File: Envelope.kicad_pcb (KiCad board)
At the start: 2 copper layers, 39.6 x 100 mm, 54 parts, among them J6 Conn_02x03_Odd_Even, J7 Conn_01x06, J8 Conn_02x05_Odd_Even, SW1 RST, U1 TL072, U2 ATmega328PB-AU, U3 L7805, Y1 Crystal

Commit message: Finished schema and footprint assignments.
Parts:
- removed J6: Conn_02x03_Odd_Even, Pin_Headers:Pin_Header_Straight_2x03_Pitch2.54mm
- removed J7: Conn_01x06, Pin_Headers:Pin_Header_Straight_1x06_Pitch2.54mm
- removed J8: Conn_02x05_Odd_Even, Pin_Headers:Pin_Header_Straight_2x05_Pitch2.54mm
- added C14: 100n, Capacitor_SMD:C_0805_2012Metric, F.Cu at (167.3, 45.5)
- added C15: 10u, Capacitor_SMD:CP_Elec_4x5.8, F.Cu at (162.2, 44.7)
- added C16: 100n, Capacitor_SMD:C_0805_2012Metric, F.Cu at (189.5, 50.0)
- added C17: 100n, Capacitor_SMD:C_0805_2012Metric, F.Cu at (199.1, 44.0)
- added C18: 100n, Capacitor_SMD:C_0805_2012Metric, F.Cu at (192.9, 48.1)
- added C19: 22p, Capacitor_SMD:C_0805_2012Metric, F.Cu at (192.9, 50.0)
- added C20: 22p, Capacitor_SMD:C_0805_2012Metric, F.Cu at (199.1, 40.5)
- added D10: LED, LED_THT:LED_D3.0mm, F.Cu at (192.4, 63.6)
- added D11: LED, LED_THT:LED_D3.0mm, F.Cu at (192.4, 59.1)
- added D12: LED, LED_THT:LED_D3.0mm, F.Cu at (197.3, 59.1)
- added D13: LED, LED_SMD:LED_1206_3216Metric_Castellated, F.Cu at (193.8, 55.7)
- added D9: LED, LED_SMD:LED_1206_3216Metric_Castellated, F.Cu at (168.1, 43.3)
- added J1: Conn_02x05_Odd_Even, Connector_PinHeader_2.54mm:PinHeader_2x05_P2.54mm_Vertical, F.Cu at (147.7, 39.2)
- added J2: Conn_02x03_Odd_Even, Connector_PinHeader_2.54mm:PinHeader_2x03_P2.54mm_Vertical, F.Cu at (203.3, 36.1)
- added J3: Conn_01x06, Connector_PinHeader_2.54mm:PinHeader_1x06_P2.54mm_Vertical, F.Cu at (186.0, 36.1)
- added R16: 100k, Resistor_SMD:R_0805_2012Metric, F.Cu at (128.7, 51.1)
- added R17: 1k, Resistor_SMD:R_0805_2012Metric, F.Cu at (119.0, 63.2)
- added R18: 47k, Resistor_SMD:R_0805_2012Metric, F.Cu at (123.7, 58.6)
- added R19: 47k, Resistor_SMD:R_0805_2012Metric, F.Cu at (135.9, 44.2)
- added R20: 47k, Resistor_SMD:R_0805_2012Metric, F.Cu at (132.3, 48.7)
- added R21: 100k, Resistor_SMD:R_0805_2012Metric, F.Cu at (140.7, 39.6)
- added R22: 1k, Resistor_SMD:R_0805_2012Metric, F.Cu at (120.1, 54.1)
- added R23: 330, Resistor_SMD:R_0805_2012Metric, F.Cu at (164.0, 49.4)
- added R24: 330, Resistor_SMD:R_0805_2012Metric, F.Cu at (202.8, 57.4)
- added R25: 330, Resistor_SMD:R_0805_2012Metric, F.Cu at (198.0, 55.5)
- added R26: 330, Resistor_SMD:R_0805_2012Metric, F.Cu at (201.4, 55.5)
- added R27: 10k, Resistor_SMD:R_0805_2012Metric, F.Cu at (189.5, 48.1)
- added R28: 330, Resistor_SMD:R_0805_2012Metric, F.Cu at (197.9, 62.3)
- added SW2: SW_SPDT_MSM, Local:SP1MS1, F.Cu at (189.5, 60.2)
- added SW3: SW_Push, Button_Switch_THT:SW_PUSH_6mm_H9.5mm, F.Cu at (189.3, 41.1)
- C1, C2, C3: value C -> 47n; footprint Capacitors_SMD:C_0805 -> Capacitor_SMD:C_0805_2012Metric; moved to F.Cu
- C10, C5: footprint Capacitors_SMD:C_0805 -> Capacitor_SMD:C_0805_2012Metric; moved to F.Cu
- C11: value 100n -> 10u; footprint Capacitors_SMD:C_0805 -> Capacitor_SMD:CP_Elec_4x5.8; moved to F.Cu
- C12: footprint Capacitors_SMD:CP_Elec_4x5.8 -> Capacitor_SMD:CP_Elec_4x5.8; moved to F.Cu
- C13, C9: value 10u -> 100n; footprint Capacitors_SMD:CP_Elec_4x5.8 -> Capacitor_SMD:C_0805_2012Metric; moved to F.Cu
- C4: value 100n -> 47n; footprint Capacitors_SMD:C_0805 -> Capacitor_SMD:C_0805_2012Metric; moved to F.Cu
- C6: value 100n -> 470p; footprint Capacitors_SMD:C_0805 -> Capacitor_SMD:C_0805_2012Metric; moved to F.Cu
- C7: value 22p -> 100n; footprint Capacitors_SMD:C_0805 -> Capacitor_SMD:C_0805_2012Metric; moved to F.Cu
- C8: value 22p -> 470p; footprint Capacitors_SMD:C_0805 -> Capacitor_SMD:C_0805_2012Metric; moved to F.Cu
- D1, D2, D3, D4, D5, D6: footprint Diodes_SMD:D_SOD-123 -> Diode_SMD:D_SOD-123; moved to F.Cu
- D7, D8: footprint Diodes_SMD:D_PowerDI-123 -> Diode_SMD:D_PowerDI-123; moved to F.Cu
- R1, R3: value 47k -> 33k; footprint Resistors_SMD:R_0805 -> Resistor_SMD:R_0805_2012Metric; moved to F.Cu
- R10, R9: value 100k -> 1k; footprint Resistors_SMD:R_0805 -> Resistor_SMD:R_0805_2012Metric; moved to F.Cu
- R11: value 1k -> 47k; footprint Resistors_SMD:R_0805 -> Resistor_SMD:R_0805_2012Metric; moved to F.Cu
- R12: value 100k -> 47k; footprint Resistors_SMD:R_0805 -> Resistor_SMD:R_0805_2012Metric; moved to F.Cu
- R13, R8: footprint Resistors_SMD:R_0805 -> Resistor_SMD:R_0805_2012Metric; moved to F.Cu
- R14: value 4k7 -> 47k; footprint Resistors_SMD:R_0805 -> Resistor_SMD:R_0805_2012Metric; moved to F.Cu
- R15: value 10k -> 47k; footprint Resistors_SMD:R_0805 -> Resistor_SMD:R_0805_2012Metric; moved to F.Cu
- R2, R4: value 4k7 -> 33k; footprint Resistors_SMD:R_0805 -> Resistor_SMD:R_0805_2012Metric; moved to F.Cu
- R5, R6: value R -> 33k; footprint Resistors_SMD:R_0805 -> Resistor_SMD:R_0805_2012Metric; moved to F.Cu
- R7: value R -> 1k; footprint Resistors_SMD:R_0805 -> Resistor_SMD:R_0805_2012Metric; moved to F.Cu
- RV1, RV2, RV3, RV4, RV5: value POT -> 100k; footprint Potentiometers:Potentiometer_Alps_RK09K_Horizontal -> Local:AlpsRK09K
- SW1: value RST -> SW_SPDT_MSM; footprint Buttons_Switches_THT:SW_PUSH_6mm_h13mm -> Local:SP1MS1; moved to F.Cu
- U1: footprint Housings_SSOP:OnSemi_Micro8 -> Package_SO:TSSOP-8_3x3mm_P0.65mm; moved to F.Cu
- U2: footprint Housings_QFP:LQFP-32_7x7mm_Pitch0.8mm -> Package_QFP:TQFP-32_7x7mm_P0.8mm; moved to F.Cu
- U3: footprint TO_SOT_Packages_SMD:TO-263-2 -> Package_TO_SOT_THT:TO-220-3_Vertical; moved to F.Cu
- Y1: value Crystal -> 20MHz; footprint Crystals:Crystal_SMD_5032-2pin_5.0x3.2mm -> Crystal:Crystal_SMD_HC49-SD; moved to F.Cu
- moved D5 135.5 mm to (94.0, 67.4), turned to 0 degrees
- moved D4 132.0 mm to (89.2, 67.4), turned to 0 degrees
- moved D1 126.6 mm to (98.7, 67.4), turned to 0 degrees
- moved R8 121.7 mm to (133.5, 39.6), turned to 0 degrees
- moved R9 121.7 mm to (128.7, 46.5), turned to 0 degrees
- moved D2 119.1 mm to (115.9, 55.3), turned to 0 degrees
- moved D6 116.0 mm to (115.9, 53.0), turned to 0 degrees
- moved R12 115.6 mm to (137.1, 39.6), turned to 0 degrees
- moved D3 115.3 mm to (129.3, 38.5), turned to 0 degrees
- moved C4 115.2 mm to (132.2, 52.0), turned to 0 degrees
- moved R6 113.6 mm to (128.7, 42.0), turned to 0 degrees
- moved R4 113.3 mm to (139.6, 44.2), turned to 0 degrees
- moved R5 113.2 mm to (127.3, 55.6), turned to 0 degrees
- moved R7 111.3 mm to (115.4, 58.8), turned to 0 degrees
- moved C7 110.4 mm to (102.8, 67.2), turned to 0 degrees
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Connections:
- C10 pad 1: +12V -> GND
- C10 pad 2: GND -> -12V
- C11 pad 1: +5V -> +12V
- C12 pad 1: +5V -> GND
- C12 pad 2: GND -> -12V
- C13 pad 1: GND -> +12V
- C13 pad 2: -12V -> GND
- C4 pad 1: +5V -> Net-(C4-Pad1)
- C5 pad 1: GND -> Net-(C5-Pad1)
- C5 pad 2: +5V -> GND
- C6 pad 2: GND -> Net-(C6-Pad2)
- C7 pad 1: GND -> Net-(C7-Pad1)
- C7 pad 2: Net-(C7-Pad2) -> GND
- C8 pad 1: GND -> Net-(C8-Pad1)
- J-Gate1 pad TN: Net-(J-Gate1-PadTN) -> +5V
- J-Trig1 pad TN: Net-(J-Trig1-PadTN) -> +5V
- R10 pad 1: Net-(R10-Pad1) -> Net-(C4-Pad1)
- R10 pad 2: GND -> Net-(C3-Pad1)
- R11 pad 1: Net-(J-Inv1-PadT) -> Net-(C7-Pad1)
- R11 pad 2: Net-(R11-Pad2) -> +5V
- R12 pad 1: Net-(R11-Pad2) -> Net-(C5-Pad1)
- R12 pad 2: GND -> +5V
- R13 pad 1: Net-(D5-Pad2) -> Net-(C6-Pad2)
- R13 pad 2: Net-(J-CV1-PadT) -> Net-(C4-Pad1)
- R14 pad 1: /MCU328/PC5 -> GND
- R14 pad 2: Net-(D5-Pad2) -> Net-(C5-Pad1)
- R15 pad 1: +5V -> Net-(C6-Pad1)
- R15 pad 2: Net-(J6-Pad1) -> Net-(C6-Pad2)
- R2 pad 1: /MCU328/PB0 -> Net-(D3-Pad2)
- R2 pad 2: Net-(D1-Pad2) -> Net-(J-Trig1-PadT)
- R3 pad 1: Net-(D3-Pad2) -> Net-(D5-Pad2)
- R3 pad 2: Net-(J-Trig1-PadT) -> Net-(J-CV1-PadT)
- R4 pad 1: /MCU328/PB2 -> /MCU328/PB0
- R4 pad 2: Net-(D3-Pad2) -> Net-(D1-Pad2)
- R5 pad 1: Net-(C1-Pad1) -> /MCU328/PB2
- R5 pad 2: /MCU328/PB1 -> Net-(D3-Pad2)
- R6 pad 1: Net-(C2-Pad1) -> /MCU328/PC5
- R6 pad 2: Net-(C1-Pad1) -> Net-(D5-Pad2)
- R7 pad 1: Net-(C3-Pad1) -> Net-(C1-Pad1)
- R7 pad 2: Net-(C2-Pad1) -> /MCU328/PB1
- R8 pad 1: Net-(J-Out1-PadT) -> Net-(C2-Pad1)
- R8 pad 2: Net-(R10-Pad1) -> Net-(C1-Pad1)
- R9 pad 2: GND -> Net-(C2-Pad1)
- SW1 pad 1: Net-(J6-Pad1) -> /MCU328/PE0
- U1 pad 1: Net-(R10-Pad1) -> Net-(C6-Pad1)
- U1 pad 2: Net-(R10-Pad1) -> Net-(C6-Pad2)
- U1 pad 3: Net-(C3-Pad1) -> Net-(C5-Pad1)
- U1 pad 5: Net-(U1-Pad5) -> Net-(C7-Pad1)
- U1 pad 6: Net-(U1-Pad6) -> Net-(C8-Pad2)
- U1 pad 7: Net-(R11-Pad2) -> Net-(C8-Pad1)
- U2 pad 16: Net-(J6-Pad1) -> Net-(J2-Pad1)
- U2 pad 17: Net-(J6-Pad1) -> Net-(J2-Pad3)
- U2 pad 20: Net-(C6-Pad1) -> Net-(C16-Pad2)
- U2 pad 29: Net-(J6-Pad1) -> Net-(J2-Pad5)
- U2 pad 7: Net-(C7-Pad2) -> Net-(C19-Pad2)
- U2 pad 8: Net-(C8-Pad2) -> Net-(C20-Pad2)
- Y1 pad 1: Net-(C8-Pad2) -> Net-(C19-Pad2)
- Y1 pad 2: Net-(C7-Pad2) -> Net-(C20-Pad2)
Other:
- board outline removed
- net class Default: via_dia 0.6 -> 0.8
- rule pad_to_mask_clearance: 0.2 -> 0

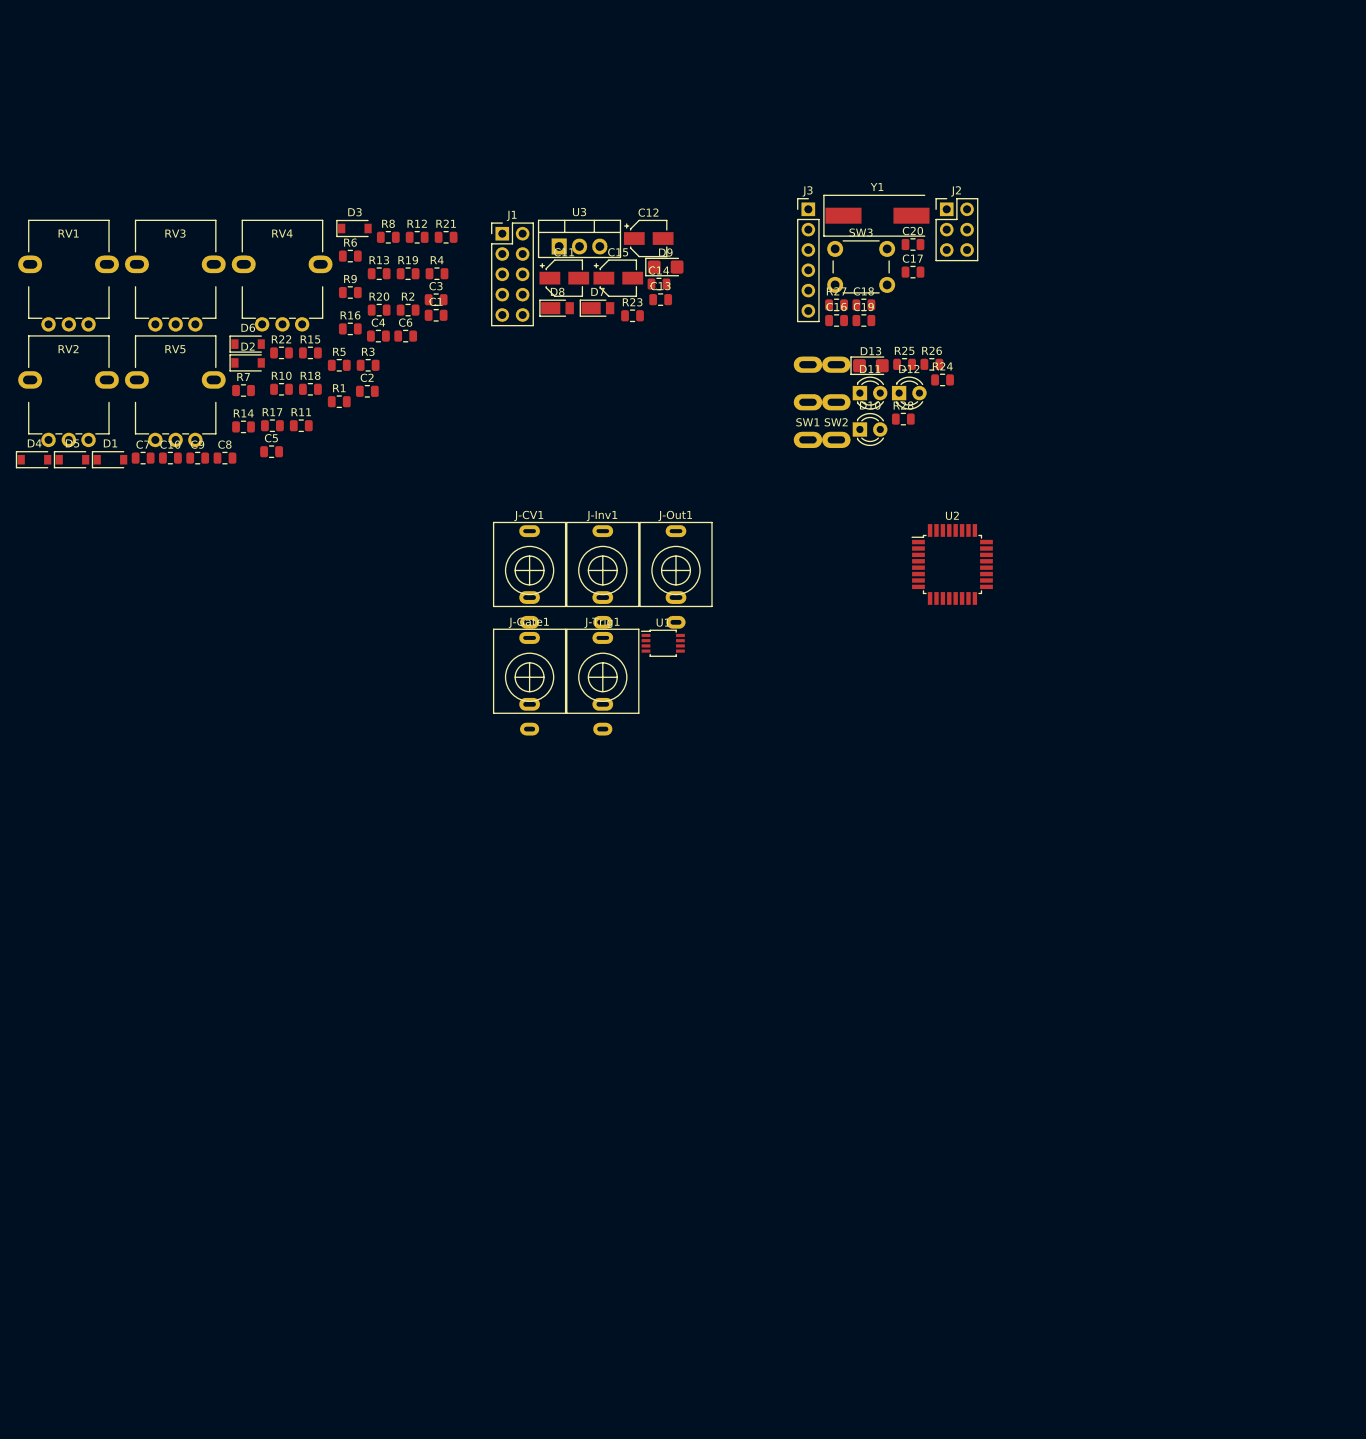
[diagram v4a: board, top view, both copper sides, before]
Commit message: All components place on board but no routing.
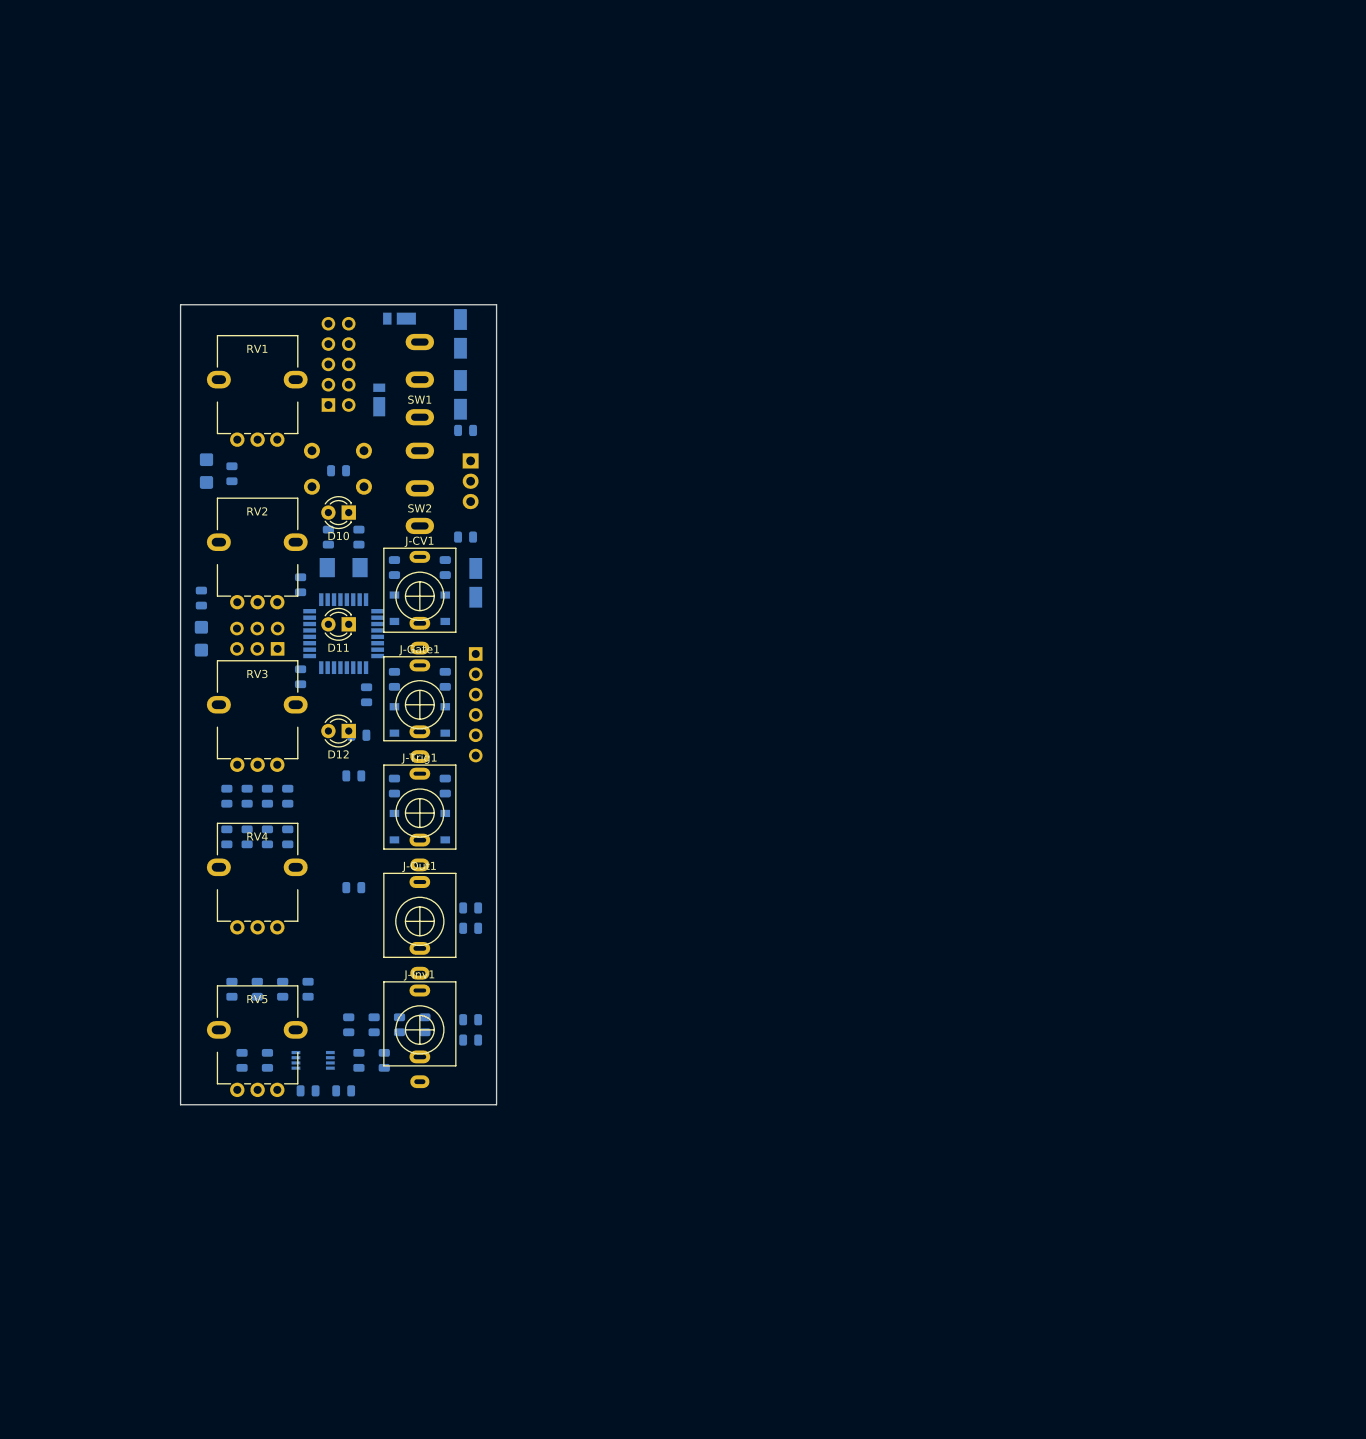
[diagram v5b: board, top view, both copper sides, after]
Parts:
- C1, C10, C11, C12, C13, C14, C15, C16, C17, C18, C19, C2, C20, C3, C4, C5, C6, C7, C8, C9, D1, D13, D2, D3, D4, D5, D6, D7, D8, D9, J1, J2, J3, R1, R10, R11, R12, R13, R14, R15, R16, R17, R18, R19, R2, R20, R21, R22, R23, R24, R25, R26, R27, R28, R3, R4, R5, R6, R7, R8, R9, SW3, U1, U2, U3: moved to B.Cu
- Y1: footprint Crystal:Crystal_SMD_HC49-SD -> Crystal:Crystal_SMD_Abracon_ABM3-2Pin_5.0x3.2mm; moved to B.Cu
- moved J2 100.1 mm to (119.6, 91.1), turned to 90 degrees
- moved R12 98.8 mm to (128.5, 138.0), turned to 270 degrees
- moved R24 97.2 mm to (129.2, 120.9), turned to 180 degrees
- moved R20 94.8 mm to (118.4, 142.5), turned to 270 degrees
- moved R13 94.1 mm to (138.0, 138.0), turned to 270 degrees
- moved R19 91.4 mm to (117.1, 133.6), turned to 90 degrees
- moved C6 90.6 mm to (133.0, 142.5), turned to 270 degrees
- moved R28 90.6 mm to (110.1, 84.7), turned to 270 degrees
- moved D13 90.4 mm to (110.1, 89.8), turned to 90 degrees
- moved R15 88.6 mm to (129.8, 142.5), turned to 270 degrees
- moved R16 87.7 mm to (143.8, 137.4)
- moved C17 86.3 mm to (130.8, 96.8), turned to 270 degrees
- moved R25 85.9 mm to (129.2, 106.9), turned to 180 degrees
- moved R26 85.3 mm to (129.8, 101.9), turned to 180 degrees
- moved R21 83.9 mm to (143.8, 123.4)
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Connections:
- C1 pad 2: GND -> (no net)
- C10 pad 1: GND -> (no net)
- C11 pad 2: GND -> (no net)
- C12 pad 1: GND -> (no net)
- C13 pad 2: GND -> (no net)
- C14 pad 2: GND -> (no net)
- C15 pad 2: GND -> (no net)
- C16 pad 1: GND -> (no net)
- C17 pad 2: GND -> (no net)
- C18 pad 1: GND -> (no net)
- C19 pad 1: GND -> (no net)
- C2 pad 2: GND -> (no net)
- C20 pad 1: GND -> (no net)
- C3 pad 2: GND -> (no net)
- C4 pad 2: GND -> (no net)
- C5 pad 2: GND -> (no net)
- C7 pad 2: GND -> (no net)
- C9 pad 2: GND -> (no net)
- D10 pad 1: GND -> (no net)
- D11 pad 1: GND -> (no net)
- D12 pad 1: GND -> (no net)
- D13 pad 1: GND -> (no net)
- D2 pad 2: GND -> (no net)
- D4 pad 2: GND -> (no net)
- D6 pad 2: GND -> (no net)
- D9 pad 1: GND -> (no net)
- J-CV1 pad S: GND -> (no net)
- J-Gate1 pad S: GND -> (no net)
- J-Inv1 pad S: GND -> (no net)
- J-Out1 pad S: GND -> (no net)
- J-Trig1 pad S: GND -> (no net)
- J1 pad 1: Net-(D7-Pad2) -> Net-(D8-Pad1)
- J1 pad 10: Net-(D8-Pad1) -> Net-(D7-Pad2)
- J1 pad 2: Net-(D7-Pad2) -> Net-(D8-Pad1)
- J1 pad 3: GND -> (no net)
- J1 pad 4: GND -> (no net)
- J1 pad 5: GND -> (no net)
- J1 pad 6: GND -> (no net)
- J1 pad 7: GND -> (no net)
- J1 pad 8: GND -> (no net)
- J1 pad 9: Net-(D8-Pad1) -> Net-(D7-Pad2)
- J2 pad 6: GND -> (no net)
- J3 pad 1: GND -> (no net)
- R14 pad 1: GND -> (no net)
- R16 pad 2: GND -> (no net)
- R19 pad 1: GND -> (no net)
- R21 pad 2: GND -> (no net)
- RV1 pad 3: GND -> (no net)
- RV2 pad 3: GND -> (no net)
- RV3 pad 3: GND -> (no net)
- RV4 pad 3: GND -> (no net)
- RV5 pad 3: GND -> (no net)
- SW1 pad 2: GND -> (no net)
- SW2 pad 2: GND -> (no net)
- SW3 pad 2: GND -> (no net)
- U2 pad 21: GND -> (no net)
- U2 pad 5: GND -> (no net)
- U3 pad 2: GND -> (no net)
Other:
- board outline added: 39.5 x 100 mm

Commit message: More adjustments on placement.
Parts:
- moved D10 51.1 mm to (128.5, 125.1)
- moved J3 46.0 mm to (109.9, 61.3)
- moved D13 38.4 mm to (115.2, 51.7), turned to 270 degrees
- moved R28 28.6 mm to (118.6, 57.4), turned to 90 degrees
- moved D11 23.6 mm to (128.5, 111.6)
- moved D9 17.1 mm to (110.7, 51.7), turned to 270 degrees
- moved C10 12.1 mm to (118.7, 138.4), turned to 90 degrees
- moved R23 11.9 mm to (115.4, 57.4), turned to 90 degrees
- moved C9 11.2 mm to (115.5, 138.4), turned to 270 degrees
- moved R15 9.42 mm to (126.3, 133.7)
- moved C6 9.42 mm to (129.5, 133.7)
- moved C8 9.42 mm to (111.7, 133.7)
- moved R20 9.42 mm to (114.9, 133.7)
- moved U1 9.42 mm to (120.6, 133.7)
- moved R21 7.47 mm to (136.4, 124.5), turned to 90 degrees
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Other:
- net class Default: clearance 0.2 -> 0.254; trace_width 0.25 -> 0.254
- rule trace_clearance: 0.2 -> 0.254

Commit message: Started routing.
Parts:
- moved J2 6.02 mm to (111.8, 86.1), turned to 180 degrees
- moved R15 5.76 mm to (130.1, 129.4)
- moved C6 5.76 mm to (133.3, 129.4)
- moved C8 5.76 mm to (115.5, 129.4)
- moved R20 5.76 mm to (118.7, 129.4)
- moved U1 5.76 mm to (124.4, 129.4)
- moved C7 4.84 mm to (121.9, 133.9)
- moved R11 4.84 mm to (125.1, 133.9)
- moved R18 4.84 mm to (115.5, 133.9)
- moved R19 4.84 mm to (118.7, 133.9)
- turned C1 to 270 degrees
- turned C2 to 270 degrees
- turned C3 to 270 degrees
- turned C4 to 270 degrees
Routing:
- net Net-(C6-Pad1): track 0.00 -> 18.8 mm
- net Net-(C5-Pad1): track 0.00 -> 15.3 mm
- net Net-(C6-Pad2): track 0.00 -> 15.3 mm
- net Net-(D3-Pad2): track 0.00 -> 11.3 mm
- net Net-(D1-Pad2): track 0.00 -> 11.3 mm
- net Net-(D5-Pad2): track 0.00 -> 11.3 mm
- net Net-(C8-Pad2): track 0.00 -> 9.64 mm
- net Net-(C8-Pad1): track 0.00 -> 9.53 mm
- net Net-(C7-Pad1): track 0.00 -> 9.09 mm
- net Net-(C2-Pad1): track 0.00 -> 6.52 mm
- net Net-(C3-Pad1): track 0.00 -> 6.52 mm
- net Net-(C1-Pad1): track 0.00 -> 6.52 mm
- net Net-(J-Inv1-PadT): track 0.00 -> 5.48 mm
- net Net-(J-Out1-PadT): track 0.00 -> 4.35 mm
- net Net-(J-Gate1-PadT): track 0.00 -> 3.51 mm
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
